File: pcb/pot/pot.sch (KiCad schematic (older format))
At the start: 22 parts, among them CON1 Valve, J1 RJ45_LEDS, J2 RJ45, P1 Sensor, Q1 IRLZ44N, Q2 2N3904, Q3 2N3904, U1 PCF8574

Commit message: Add pot PCB
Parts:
- removed J2: RJ45, Connect:RJ45_8, symbol RJ45
- added J2: Bus, Connect:RJHSE538X, symbol RJ45_LEDS-RESCUE-pot-RESCUE-pot
- J1: value RJ45_LEDS -> Bus; symbol RJ45_LEDS -> RJ45_LEDS-RESCUE-pot-RESCUE-pot
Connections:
- net GND: now also J2.4, J2.5
- net at F1.2, J1.1, J1.2: now also J2.1, J2.2
- net at C1.1, F2.2, J1.3: now also J2.3
- net at J1.6, P1.4 (P4), U1.14 (SCL): now also J2.6
- net at J1.8, Q3.1 (C), U1.15 (SDA): now also J2.8
- new net: J1.13, J2.14
- no-connect marks 12 -> 17
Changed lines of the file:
@@
 EESchema Schematic File Version 2
+LIBS:pot-rescue
 LIBS:power
 LIBS:device
@@
 $EndDescr
 $Comp
-L RJ45_LEDS J1
+L RJ45_LEDS-RESCUE-pot-RESCUE-pot J1
 U 1 1 5951851F
 P 4250 2900
 F 0 "J1" H 4250 2400 50  0000 C CNN
-F 1 "RJ45_LEDS" H 4250 3300 50  0000 C CNN
+F 1 "Bus" H 4250 3300 50  0000 C CNN
 F 2 "Connect:RJHSE538X" H 4250 2850 50  0001 C CNN
 F 3 "" H 4250 2850 50  0000 C CNN
@@
 $EndComp
 NoConn ~ 4550 3400
-$Comp
-L RJ45 J2
-U 1 1 595189F3
-P 2850 3000
-F 0 "J2" H 3050 3500 50  0000 C CNN
-F 1 "RJ45" H 2700 3500 50  0000 C CNN
-F 2 "Connect:RJ45_8" H 2850 3000 50  0001 C CNN
-F 3 "" H 2850 3000 50  0000 C CNN
-	1    2850 3000
-	1    0    0    -1
-$EndComp
 $Comp
 L +12V #PWR01
@@
 	1    0    0    -1
 $EndComp
-NoConn ~ 3100 3450
-NoConn ~ 3400 2650
 $Comp
 L PCF8574 U1
@@
 	1    0    0    -1
 $EndComp
-Wire Wire Line
-	1400 3600 1850 3600
-Wire Wire Line
-	2350 3600 3950 3600
-Wire Wire Line
-	3850 3600 3850 3400
-Wire Wire Line
-	3950 3600 3950 3400
-Connection ~ 3850 3600
-Wire Wire Line
-	4050 3900 4050 3400
-Wire Wire Line
-	1400 4200 4350 4200
-Wire Wire Line
-	4150 4200 4150 3400
-Wire Wire Line
-	4350 4200 4350 3400
-Connection ~ 4150 4200
-Wire Wire Line
-	2500 3600 2500 3450
-Wire Wire Line
-	2600 3600 2600 3450
-Connection ~ 2500 3600
-Wire Wire Line
-	2700 3900 2700 3450
-Wire Wire Line
-	1400 3900 1850 3900
-Wire Wire Line
-	2350 3900 4050 3900
-Wire Wire Line
-	2800 4200 2800 3450
-Wire Wire Line
-	2900 4200 2900 3450
-Connection ~ 2800 4200
-Connection ~ 1700 4200
-Connection ~ 1700 3900
-Connection ~ 1700 3600
-Wire Wire Line
-	4550 2200 4550 2400
-Wire Wire Line
-	4700 2200 4650 2200
-Wire Wire Line
-	4650 2200 4650 2400
-Wire Wire Line
-	6650 2900 6550 2900
-Wire Wire Line
-	6050 5700 6150 5700
-Wire Wire Line
-	6150 5700 6150 4650
-Wire Wire Line
-	6150 4650 5000 4650
-Wire Wire Line
-	6050 5500 6350 5500
-Wire Wire Line
-	6350 5500 6350 4650
-Wire Wire Line
-	3000 3450 3000 4400
-Wire Wire Line
-	3000 4400 6650 4400
-Wire Wire Line
-	3200 3450 3200 4300
-Wire Wire Line
-	3200 4300 6050 4300
-Wire Wire Line
-	4900 5500 5050 5500
-Wire Wire Line
-	4900 4400 4900 5500
-Connection ~ 4900 4400
-Wire Wire Line
-	5050 5600 4800 5600
-Wire Wire Line
-	4800 5600 4800 4300
-Connection ~ 4800 4300
-Wire Wire Line
-	4450 3400 4450 4400
-Connection ~ 4450 4400
-Wire Wire Line
-	5050 5800 4400 5800
-Wire Wire Line
-	4400 5800 4400 5650
-Wire Wire Line
-	4400 6150 4400 6250
-Wire Wire Line
-	4400 6250 4800 6250
-Wire Wire Line
-	4800 6250 4800 5900
-Wire Wire Line
-	4800 5900 5050 5900
-Wire Wire Line
-	4400 6600 4400 6750
-Wire Wire Line
-	4400 6750 4900 6750
-Wire Wire Line
-	4900 6750 4900 6000
-Wire Wire Line
-	4900 6000 5050 6000
-Wire Wire Line
-	3950 5550 4150 5550
-Wire Wire Line
-	4150 6050 4050 6050
-Wire Wire Line
-	4050 5550 4050 6500
-Connection ~ 4050 5550
-Wire Wire Line
-	4050 6500 4150 6500
-Connection ~ 4050 6050
-Wire Wire Line
-	8000 4150 8000 4250
-Wire Wire Line
-	7600 4100 7600 3950
-Wire Wire Line
-	7600 3950 7700 3950
-Wire Wire Line
-	6350 4650 7600 4650
-Wire Wire Line
-	7600 4650 7600 4400
-Wire Wire Line
-	8500 3950 8650 3950
-Wire Wire Line
-	8500 3500 8500 3650
-Wire Wire Line
-	8000 3750 8000 3600
-Connection ~ 8500 3600
-Wire Wire Line
-	8000 3600 8500 3600
-Wire Wire Line
-	8500 3150 8500 3200
-Wire Wire Line
-	8800 3350 8800 3450
-Wire Wire Line
-	8150 2600 8150 2500
-Wire Wire Line
-	8150 2800 8800 2800
-Wire Wire Line
-	8800 2800 8800 2950
-Connection ~ 8400 2800
-Wire Wire Line
-	4650 3400 4650 4300
-Connection ~ 4650 4300
-Wire Wire Line
-	6650 4400 6650 3200
-Wire Wire Line
-	6650 3100 6550 3100
-Wire Wire Line
-	6650 3000 6450 3000
-Wire Wire Line
-	6050 4300 6050 3000
 $Comp
 L R R6
@@
 	1    0    0    -1
 $EndComp
-Wire Wire Line
-	6250 3300 6250 3450
-Wire Wire Line
-	6250 5600 6050 5600
-Wire Wire Line
-	6250 3750 6250 5600
 $Comp
 L JUMPER JP4
@@
 	0    1    1    0
 $EndComp
-Wire Wire Line
-	5000 2200 5000 2550
-Wire Wire Line
-	5000 4650 5000 3150
 $Comp
 L BC237 Q3
@@
 	0    -1   -1   0
 $EndComp
-Connection ~ 2600 3600
-Connection ~ 2700 3900
-Connection ~ 2900 4200
 $Comp
 L FUSE F1
@@
 	1    0    0    -1
 $EndComp
+$Comp
+L RJ45_LEDS-RESCUE-pot-RESCUE-pot J2
+U 1 1 59541C7B
+P 2900 2900
+F 0 "J2" H 2900 2400 50  0000 C CNN
+F 1 "Bus" H 2900 3300 50  0000 C CNN
+F 2 "Connect:RJHSE538X" H 2900 2850 50  0001 C CNN
+F 3 "" H 2900 2850 50  0000 C CNN
+	1    2900 2900
+	1    0    0    -1
+$EndComp
+NoConn ~ 3200 3400
+NoConn ~ 3300 2400
+NoConn ~ 3200 2400
+NoConn ~ 2600 2400
+NoConn ~ 2500 2400
+Wire Wire Line
+	1400 3600 1850 3600
+Wire Wire Line
+	2350 3600 3950 3600
+Wire Wire Line
+	3850 3600 3850 3400
+Wire Wire Line
+	3950 3600 3950 3400
+Connection ~ 3850 3600
+Wire Wire Line
+	4050 3900 4050 3400
+Wire Wire Line
+	1400 4200 4350 4200
+Wire Wire Line
+	4150 4200 4150 3400
+Wire Wire Line
+	4350 4200 4350 3400
+Connection ~ 4150 4200
+Wire Wire Line
+	2500 3600 2500 3400
+Wire Wire Line
+	2600 3600 2600 3400
+Connection ~ 2500 3600
+Wire Wire Line
+	2700 3900 2700 3400
+Wire Wire Line
+	1400 3900 1850 3900
+Wire Wire Line
+	2350 3900 4050 3900
+Wire Wire Line
+	2800 4200 2800 3400
+Connection ~ 2800 4200
+Connection ~ 1700 4200
+Connection ~ 1700 3900
+Connection ~ 1700 3600
+Wire Wire Line
+	4550 2200 4550 2400
+Wire Wire Line
+	4700 2200 4650 2200
+Wire Wire Line
+	4650 2200 4650 2400
+Wire Wire Line
+	6650 2900 6550 2900
+Wire Wire Line
+	6050 5700 6150 5700
+Wire Wire Line
+	6150 5700 6150 4650
+Wire Wire Line
+	6150 4650 5000 4650
+Wire Wire Line
+	6050 5500 6350 5500
+Wire Wire Line
+	6350 5500 6350 4650
+Wire Wire Line
+	4900 5500 5050 5500
+Wire Wire Line
+	4900 4400 4900 5500
+Connection ~ 4900 4400
+Wire Wire Line
+	5050 5600 4800 5600
+Wire Wire Line
+	4800 5600 4800 4300
+Connection ~ 4800 4300
+Wire Wire Line
+	4450 3400 4450 4400
+Connection ~ 4450 4400
+Wire Wire Line
+	5050 5800 4400 5800
+Wire Wire Line
+	4400 5800 4400 5650
+Wire Wire Line
+	4400 6150 4400 6250
+Wire Wire Line
+	4400 6250 4800 6250
+Wire Wire Line
+	4800 6250 4800 5900
+Wire Wire Line
+	4800 5900 5050 5900
+Wire Wire Line
+	4400 6600 4400 6750
+Wire Wire Line
+	4400 6750 4900 6750
+Wire Wire Line
+	4900 6750 4900 6000
+Wire Wire Line
+	4900 6000 5050 6000
+Wire Wire Line
+	3950 5550 4150 5550
+Wire Wire Line
+	4150 6050 4050 6050
+Wire Wire Line
+	4050 5550 4050 6500
+Connection ~ 4050 5550
+Wire Wire Line
+	4050 6500 4150 6500
+Connection ~ 4050 6050
+Wire Wire Line
+	8000 4150 8000 4250
+Wire Wire Line
+	7600 4100 7600 3950
+Wire Wire Line
+	7600 3950 7700 3950
+Wire Wire Line
+	6350 4650 7600 4650
+Wire Wire Line
+	7600 4650 7600 4400
+Wire Wire Line
+	8500 3950 8650 3950
+Wire Wire Line
+	8500 3500 8500 3650
+Wire Wire Line
+	8000 3750 8000 3600
+Connection ~ 8500 3600
+Wire Wire Line
+	8000 3600 8500 3600
+Wire Wire Line
+	8500 3150 8500 3200
+Wire Wire Line
+	8800 3350 8800 3450
+Wire Wire Line
+	8150 2600 8150 2500
+Wire Wire Line
+	8150 2800 8800 2800
+Wire Wire Line
+	8800 2800 8800 2950
+Connection ~ 8400 2800
+Wire Wire Line
+	4650 3400 4650 4300
+Connection ~ 4650 4300
+Wire Wire Line
+	6650 4400 6650 3200
+Wire Wire Line
+	6650 3100 6550 3100
+Wire Wire Line
+	6650 3000 6450 3000
+Wire Wire Line
+	6050 4300 6050 3000
+Wire Wire Line
+	6250 3300 6250 3450
+Wire Wire Line
+	6250 5600 6050 5600
+Wire Wire Line
+	6250 3750 6250 5600
+Wire Wire Line
+	5000 2200 5000 2550
+Wire Wire Line
+	5000 4650 5000 3150
+Connection ~ 2600 3600
+Connection ~ 2700 3900
 Wire Wire Line
 	8150 2500 8500 2500
@@
 Connection ~ 2450 3900
 Connection ~ 2450 4200
+Wire Wire Line
+	3000 3400 3000 4200
+Connection ~ 3000 4200
+Wire Wire Line
+	3100 3400 3100 4400
+Wire Wire Line
+	3100 4400 6650 4400
+Wire Wire Line
+	3300 3400 3300 4300
+Wire Wire Line
+	3300 4300 6050 4300
+Wire Wire Line
+	3650 2700 3500 2700
+NoConn ~ 4850 2700
+NoConn ~ 2300 2700
 $EndSCHEMATC

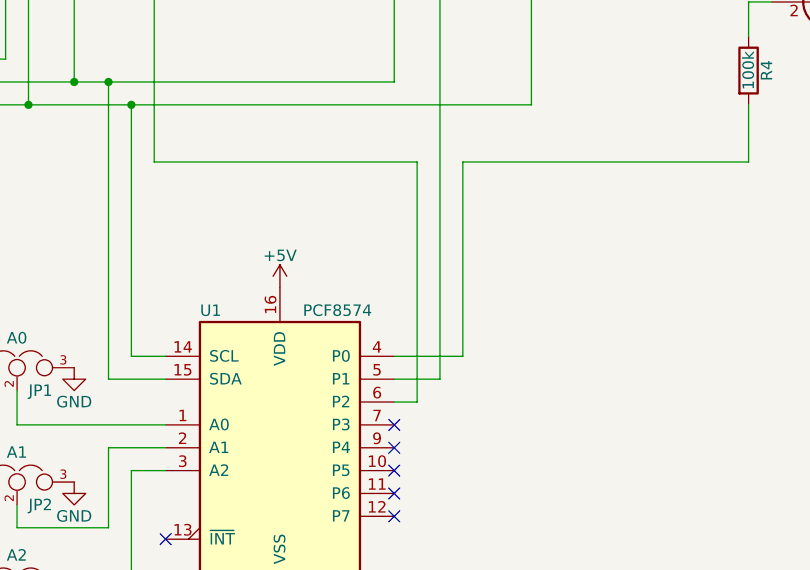
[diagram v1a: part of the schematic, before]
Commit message: Place pot LED on sensor pin
The sensor pin is most of the times LOW, so it could sink the LED's
current. When reading the sensor the LED will turn off. This will also
help as indicator to see if the pin was successfully restored to LOW
after reading the sensor. Currently the PCF8574 lib doesn't pass any
error codes further. If an LED is off, it's a good indicator for an
invalid state.
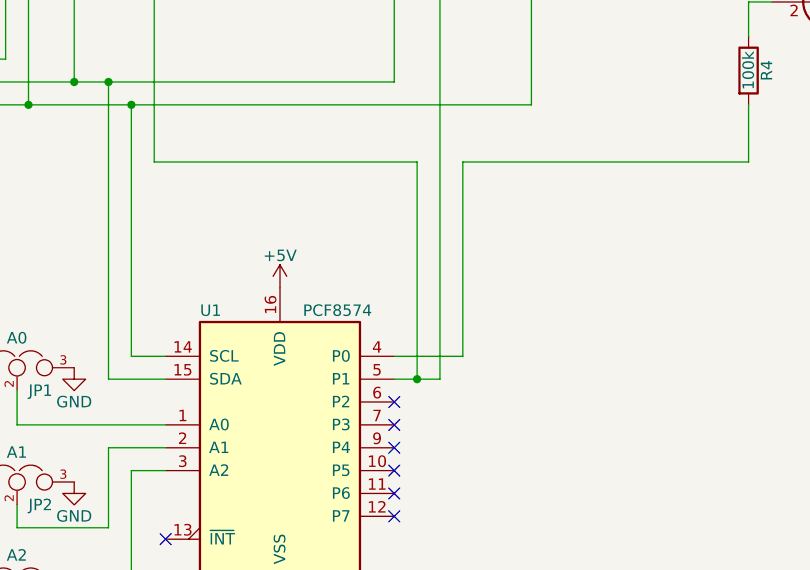
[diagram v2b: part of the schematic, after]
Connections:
- net at R6.2, U1.5 (P1): now also JP4.2
- net at U1.6 (P2): no longer JP4.2
- no-connect marks 17 -> 18
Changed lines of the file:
@@
 	6650 2900 6550 2900
-Wire Wire Line
-	6050 5700 6150 5700
-Wire Wire Line
-	6150 5700 6150 4650
 Wire Wire Line
 	6150 4650 5000 4650
@@
 NoConn ~ 4850 2700
 NoConn ~ 2300 2700
+NoConn ~ 6050 5700
+Wire Wire Line
+	6150 4650 6150 5600
+Connection ~ 6150 5600
 $EndSCHEMATC

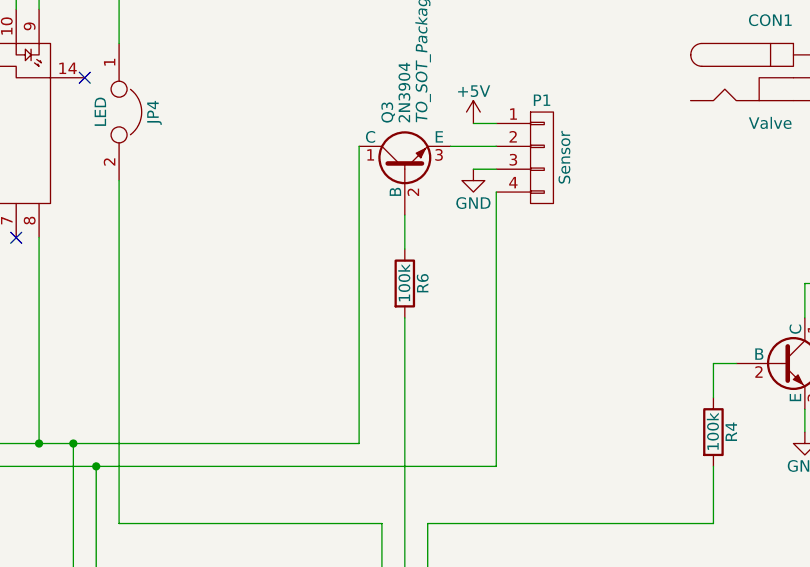
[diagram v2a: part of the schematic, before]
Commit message: Fix bus switch
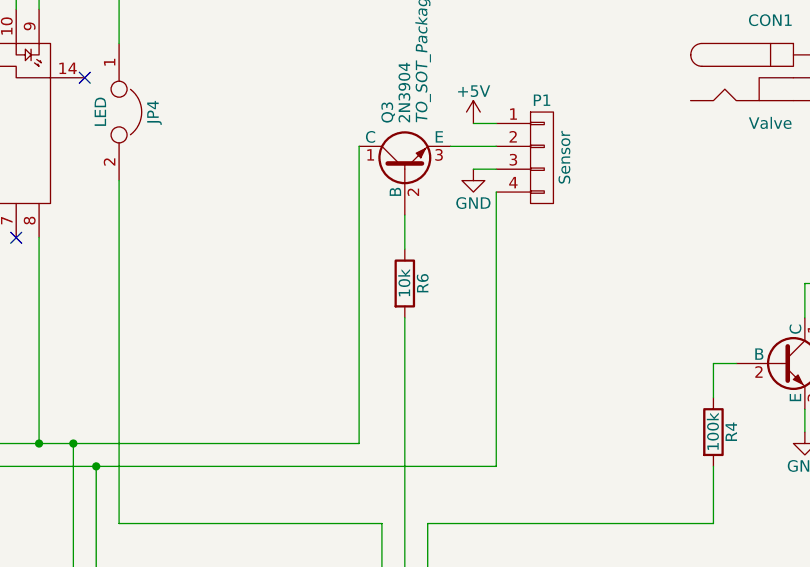
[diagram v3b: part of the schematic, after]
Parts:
- R6: value 100k -> 10k
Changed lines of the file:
@@
 P 6250 3600
 F 0 "R6" V 6330 3600 50  0000 C CNN
-F 1 "100k" V 6250 3600 50  0000 C CNN
+F 1 "10k" V 6250 3600 50  0000 C CNN
 F 2 "Resistors_ThroughHole:R_Box_L13.0mm_W4.0mm_P9.00mm" V 6180 3600 50  0001 C CNN
 F 3 "" H 6250 3600 50  0000 C CNN

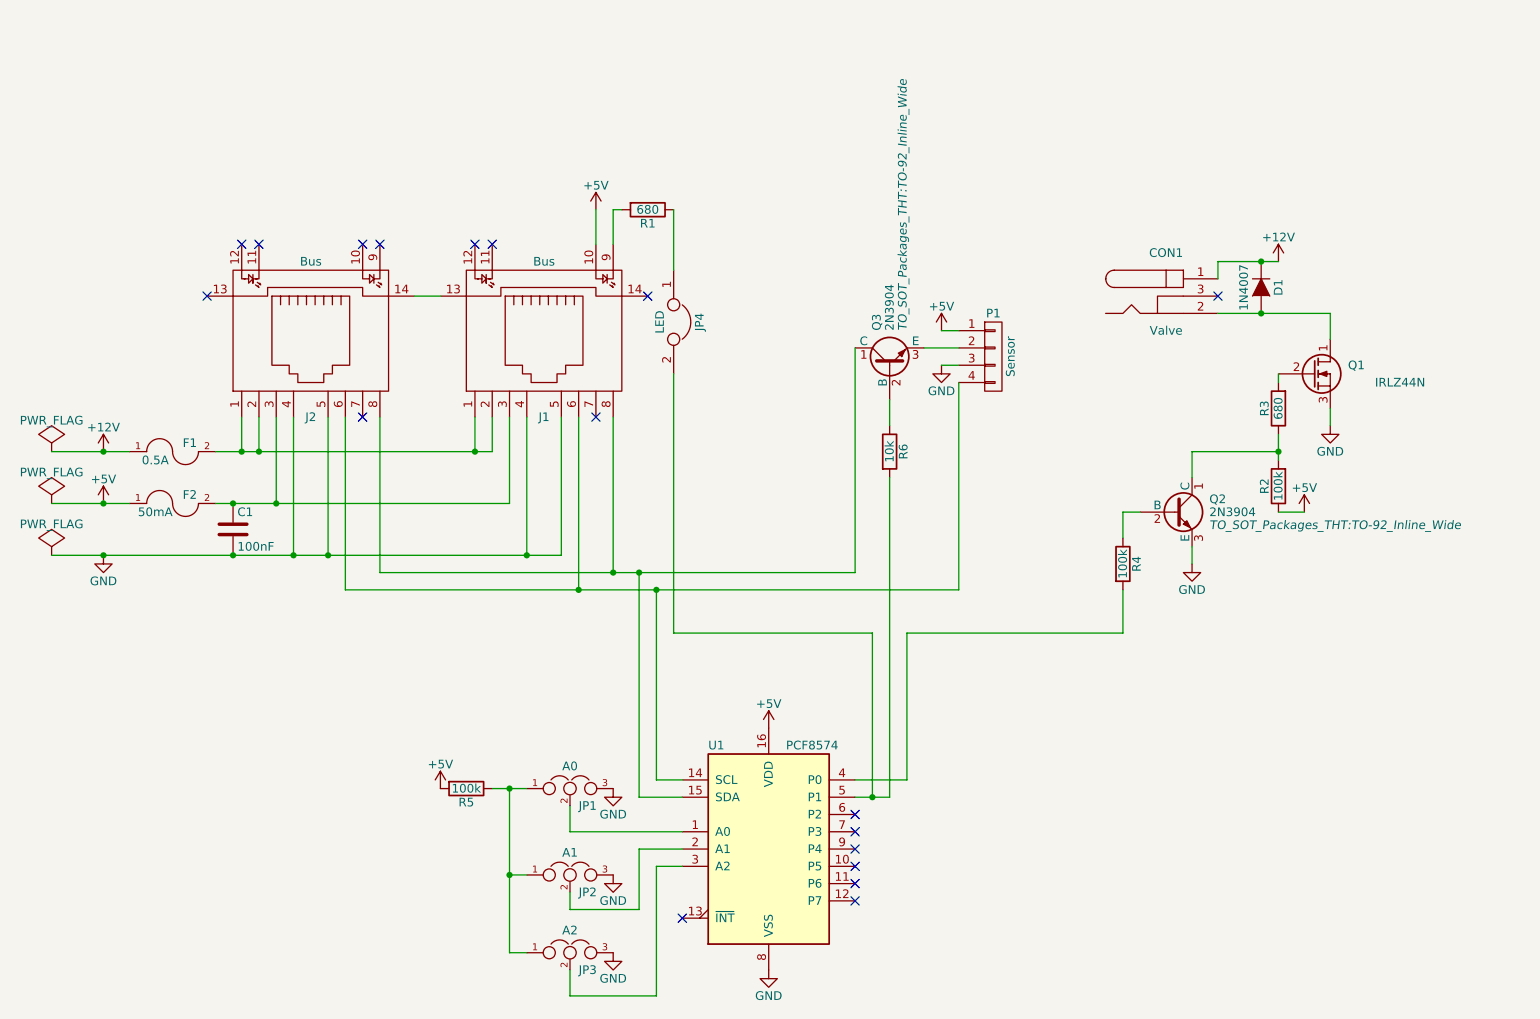
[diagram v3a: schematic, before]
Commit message: Fix bus switch
During prototyping I destroyed a bunch of N7000. It seems they're very
sensitive and need a pull down on the Gate. During prototyping I
connected the gate directly to GND or VDD. I don't know if the act of
unplugging the gate manually did destroy them or connecting them
directly. Adding a pull down resistor fixed that issue. However it might
not be necessary when using the port extender. I need to investigate
further to understand why they broke so easily.
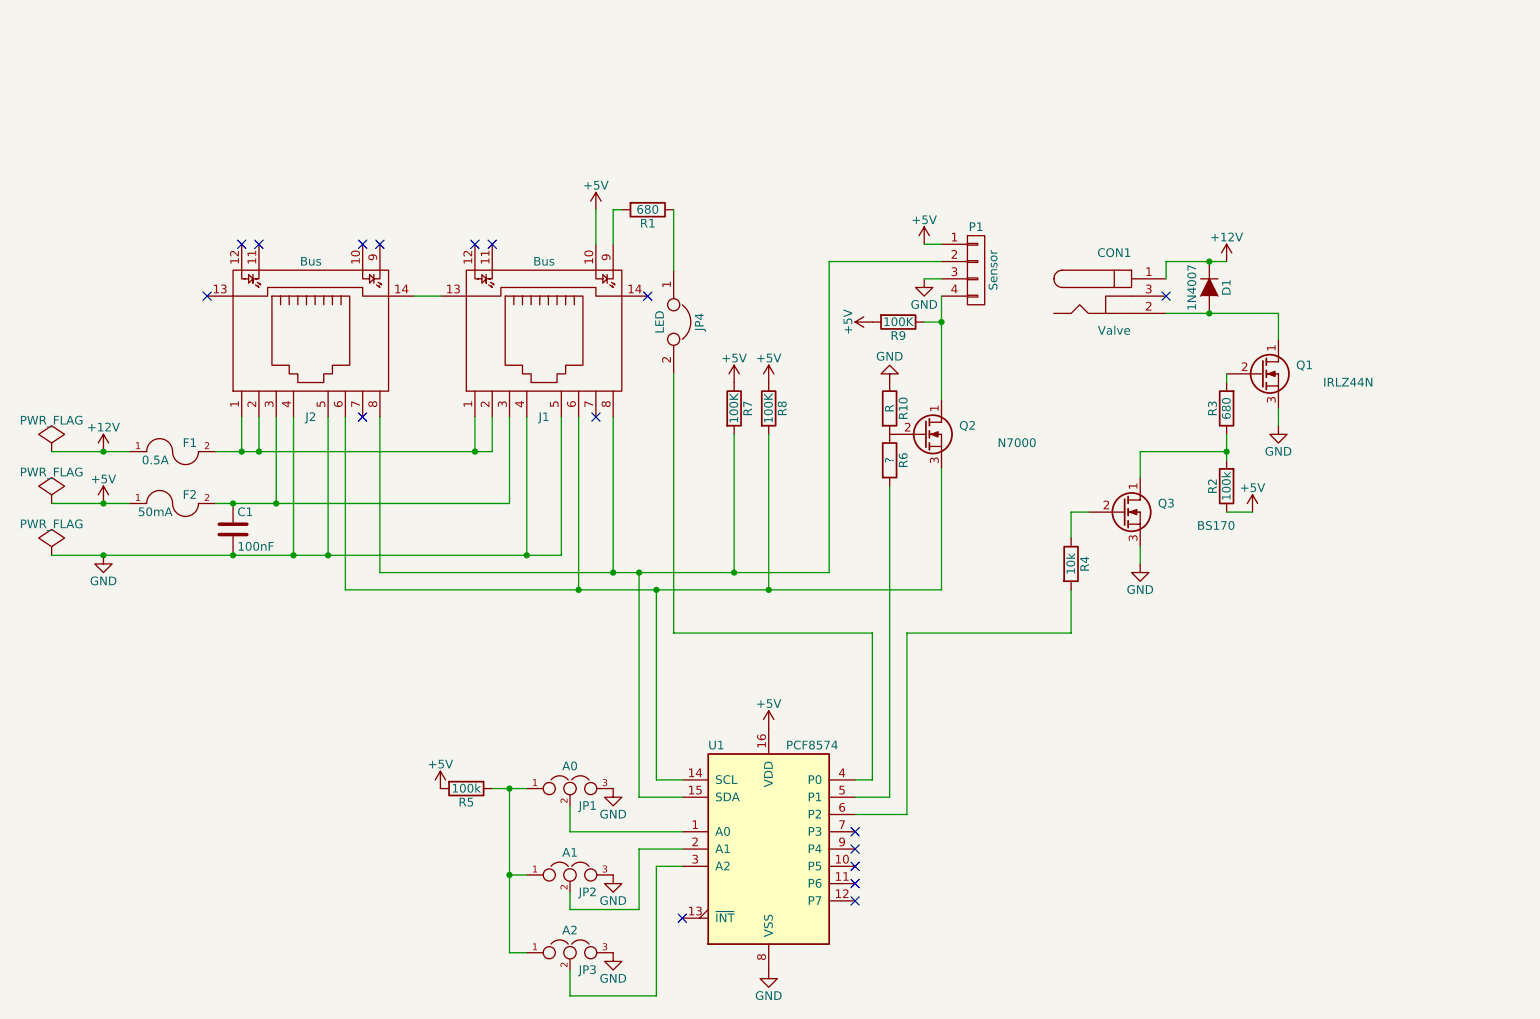
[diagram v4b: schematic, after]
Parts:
- removed Q2, Q3: 2N3904, TO_SOT_Packages_THT:TO-92_Inline_Wide, symbol BC237
- added Q2: N7000, symbol Q_NMOS_DGS
- added Q3: BS170, symbol Q_NMOS_DGS
- added R10: R, symbol R
- added R7, R8, R9: 100K, symbol R
- R4: value 100k -> 10k
- R6: value 10k -> ?
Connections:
- net +5V: now also R7.1, R8.1, R9.2
- net GND: now also Q3.3 (S), R10.1
- net at J1.6, J2.6, U1.14 (SCL): now also Q2.3 (S), R8.2; no longer P1.4 (P4)
- net at J1.8, J2.8, U1.15 (SDA): now also P1.2 (P2), R7.2
- net at U1.4 (P0): now also JP4.2; no longer R4.2
- net at R6.2, U1.5 (P1): no longer JP4.2
- net at U1.6 (P2): now also R4.2
- net at R4.1: now also Q3.2 (G)
- net at R2.2, R3.1: now also Q3.1 (D)
- net at R6.1: now also Q2.2 (G), R10.2
- new net: P1.4 (P4), Q2.1 (D), R9.1
- no-connect marks 18 -> 17
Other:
- moved on the sheet: CON1, D1, P1, Q1, R2, R3, R4, R6
